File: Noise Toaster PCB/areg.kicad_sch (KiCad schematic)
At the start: 24 parts, among them Q1 2N3906, Q9 2N5457, SW1 Manual Gate, SW2 Repeat, U2 LM324

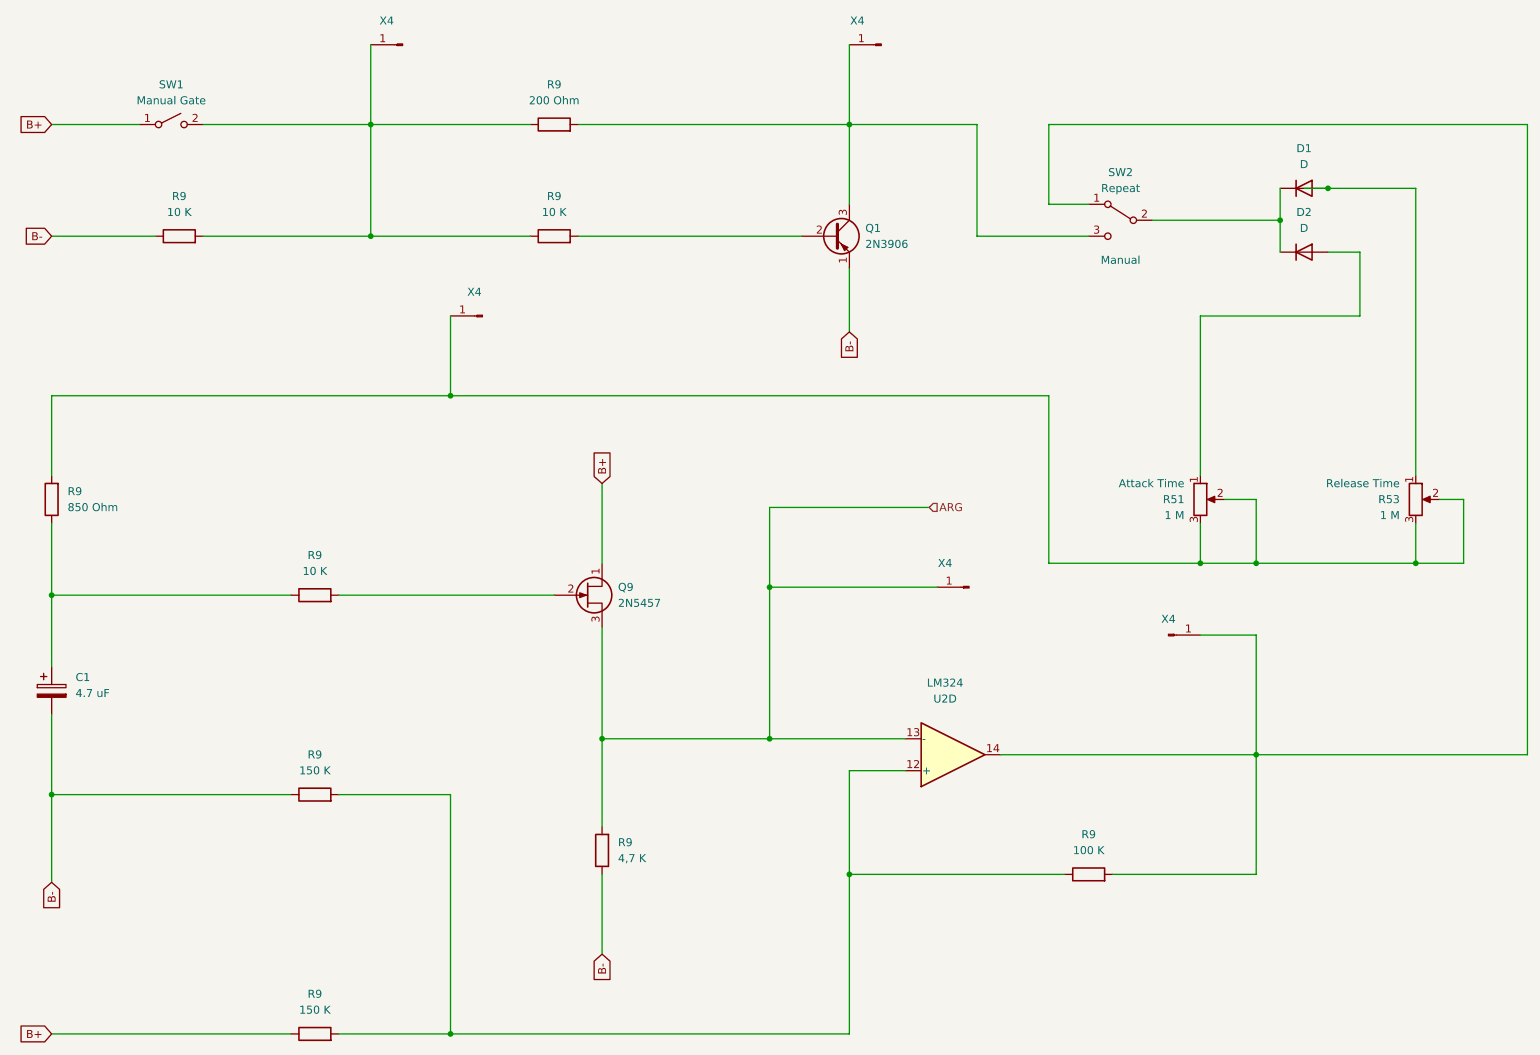
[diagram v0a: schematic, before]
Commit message: updated schematics
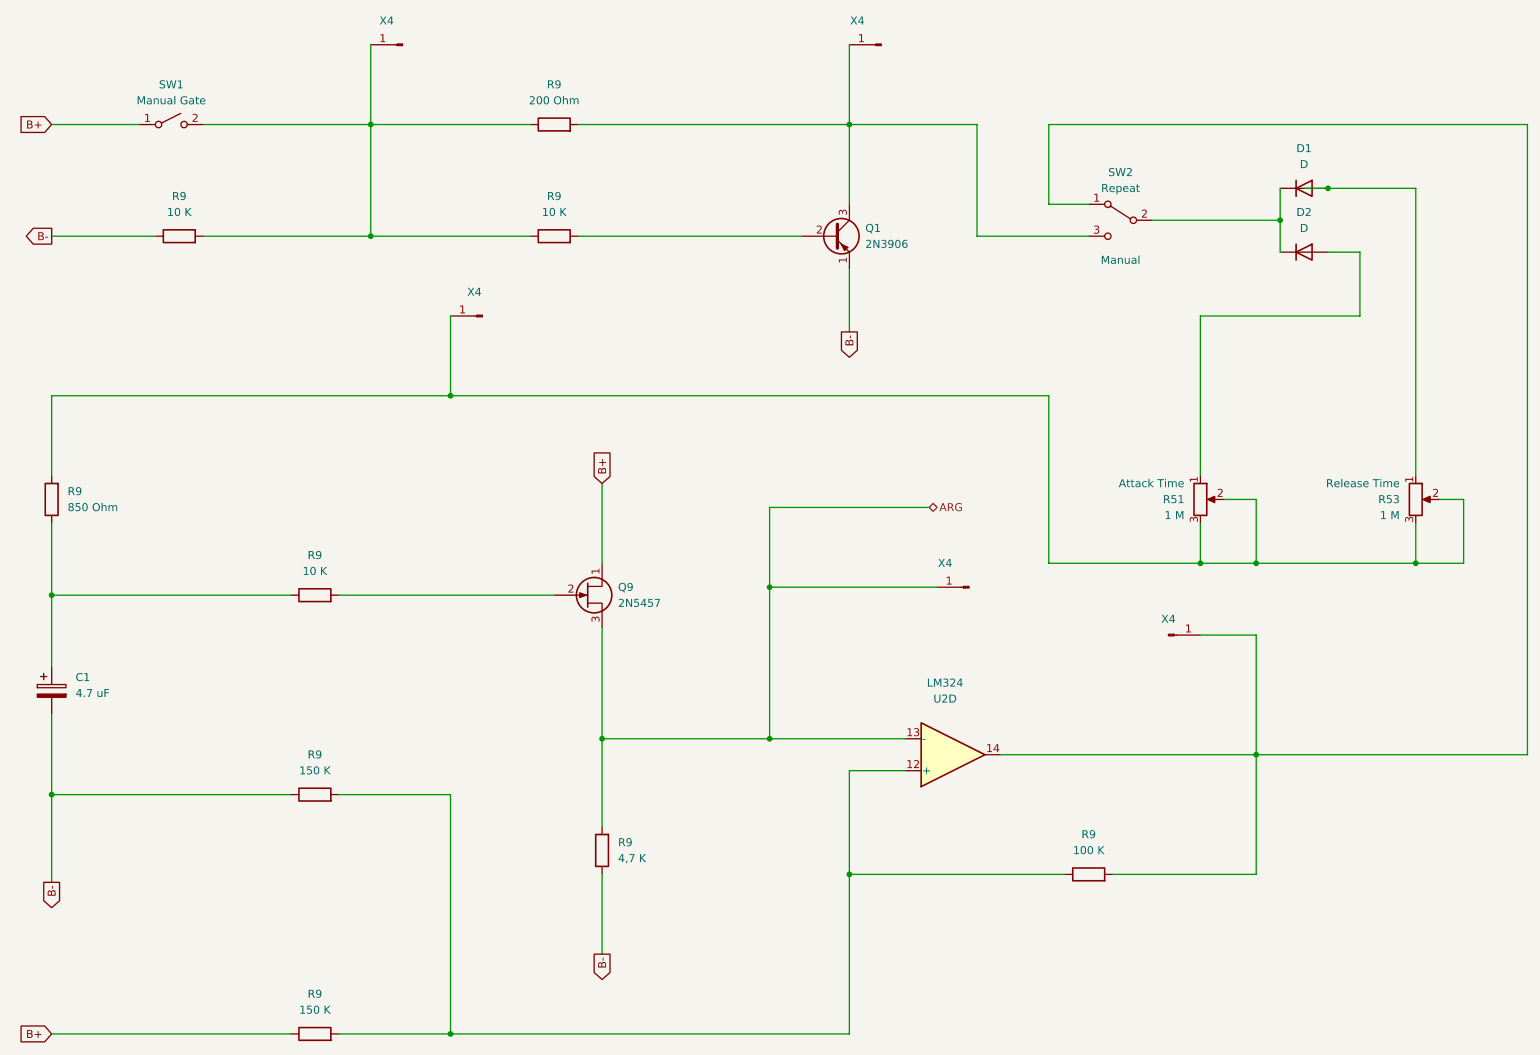
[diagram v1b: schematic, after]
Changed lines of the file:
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@@
     )
   )
-  (global_label "B-" (shape input) (at 38.1 50.8 180) (fields_autoplaced)
+  (global_label "B-" (shape output) (at 38.1 50.8 180) (fields_autoplaced)
     (effects (font (size 1.27 1.27)) (justify right))
     (property "Intersheetrefs" "${INTERSHEET_REFS}" (at 32.2724 50.8 0)
@@
     )
   )
-  (global_label "B-" (shape input) (at 165.1 66.04 270) (fields_autoplaced)
+  (global_label "B-" (shape output) (at 165.1 66.04 270) (fields_autoplaced)
     (effects (font (size 1.27 1.27)) (justify right))
     (property "Intersheetrefs" "${INTERSHEET_REFS}" (at 165.1 71.8676 90)
@@
     )
   )
-  (global_label "B-" (shape input) (at 125.73 165.1 270) (fields_autoplaced)
+  (global_label "B-" (shape output) (at 125.73 165.1 270) (fields_autoplaced)
     (effects (font (size 1.27 1.27)) (justify right))
     (property "Intersheetrefs" "${INTERSHEET_REFS}" (at 125.73 170.9276 90)
@@
     )
   )
-  (global_label "B-" (shape input) (at 38.1 153.67 270) (fields_autoplaced)
+  (global_label "B-" (shape output) (at 38.1 153.67 270) (fields_autoplaced)
     (effects (font (size 1.27 1.27)) (justify right))
     (property "Intersheetrefs" "${INTERSHEET_REFS}" (at 38.1 159.4976 90)
@@
     )
   )
-  (hierarchical_label "ARG" (shape input) (at 177.8 93.98 0) (fields_autoplaced)
+  (hierarchical_label "ARG" (shape bidirectional) (at 177.8 93.98 0) (fields_autoplaced)
     (effects (font (size 1.27 1.27)) (justify left))
   )

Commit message: refactored the schematic
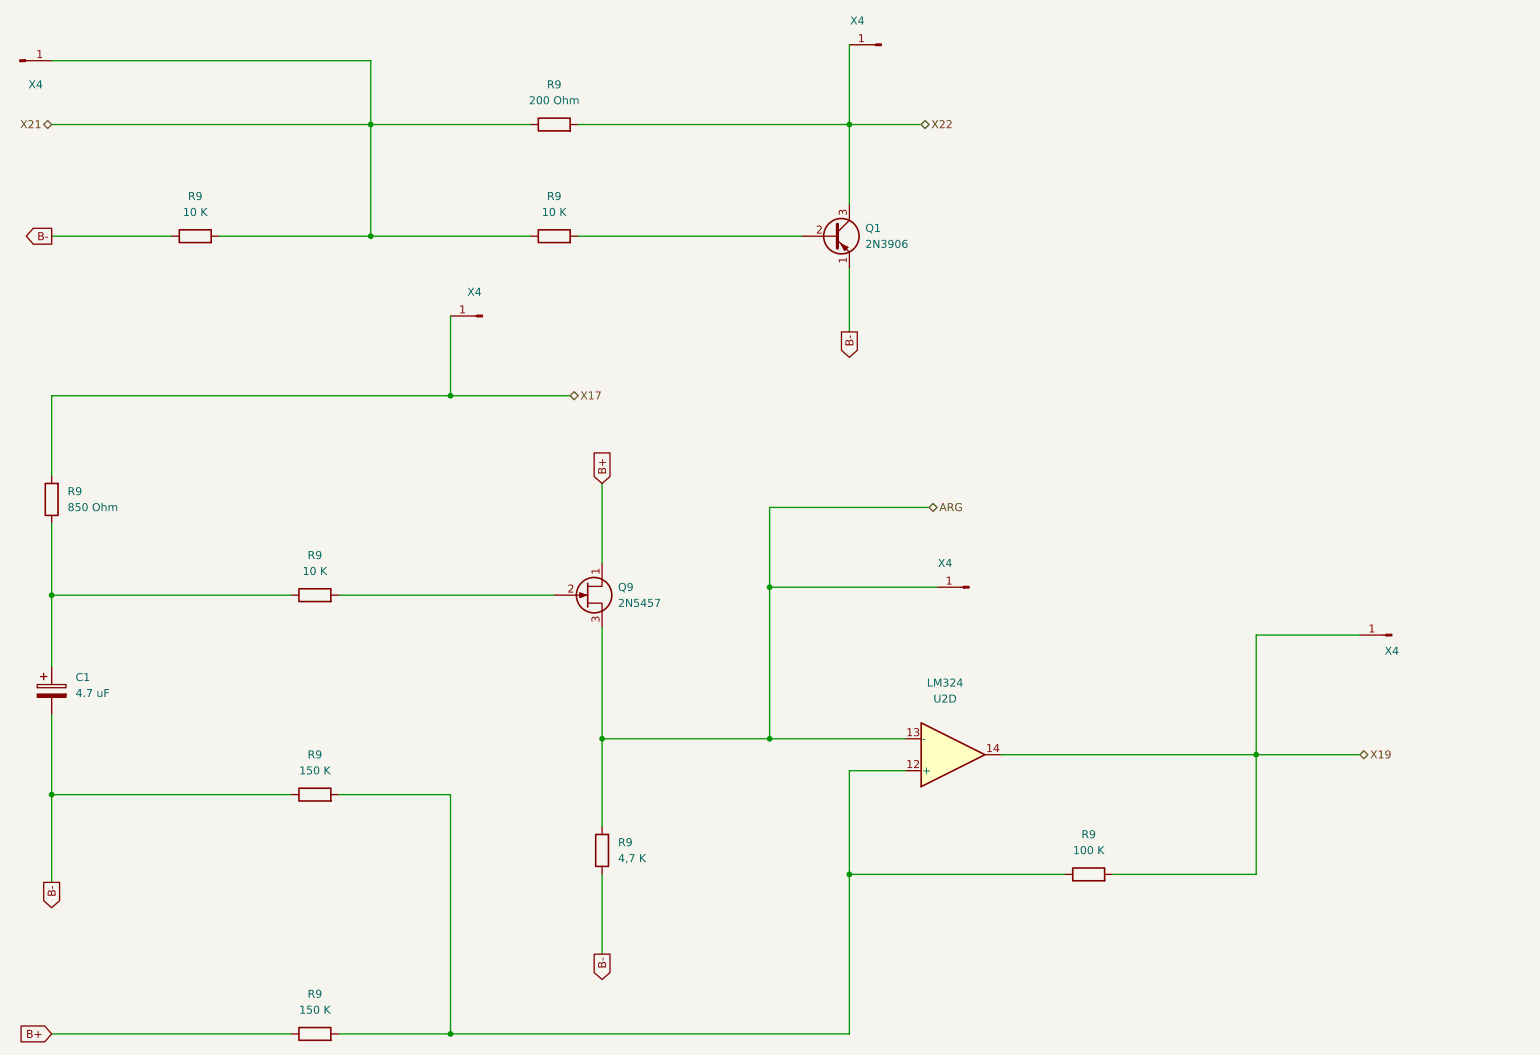
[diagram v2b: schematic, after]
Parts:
- removed D1, D2: D, symbol Device:D
- removed R51, R53: 1 M, symbol Device:R_Potentiometer
- removed SW1: Manual Gate, symbol Switch:SW_SPST
- removed SW2: Repeat, symbol Switch:SW_SPDT
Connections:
- net X21: now reaches R9.1, R9.1, R9.2, X4.1 (Pin_1)
- net X19: now reaches R9.2, U2.14, X4.1 (Pin_1)
- net X22: now reaches Q1.3 (C), R9.2, X4.1 (Pin_1)
- net X17: now reaches R9.2, X4.1 (Pin_1)
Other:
- moved on the sheet: R9, X4

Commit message: refactored schematics and added front panel
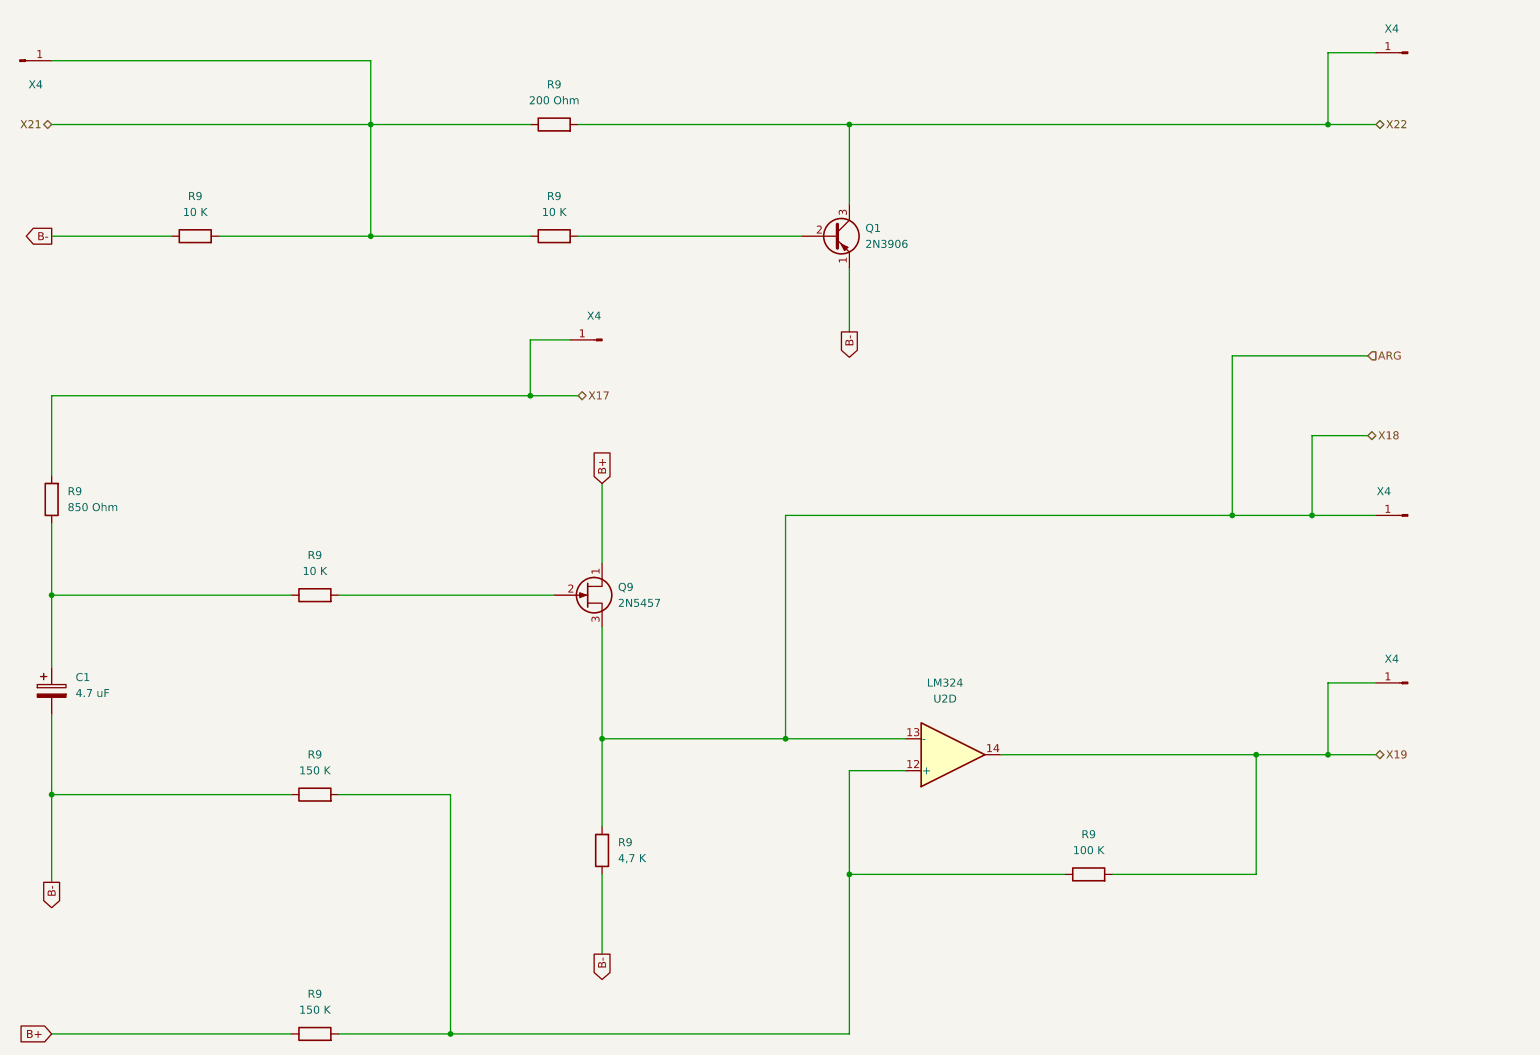
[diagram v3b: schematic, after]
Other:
- moved on the sheet: X4
